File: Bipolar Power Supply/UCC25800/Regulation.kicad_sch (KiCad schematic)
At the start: 36 parts, among them U2 LT8330_S6, U4 LT8330_S6, U5 LM317EMPX/NOPB, U6 LM337IMPX/NOPB

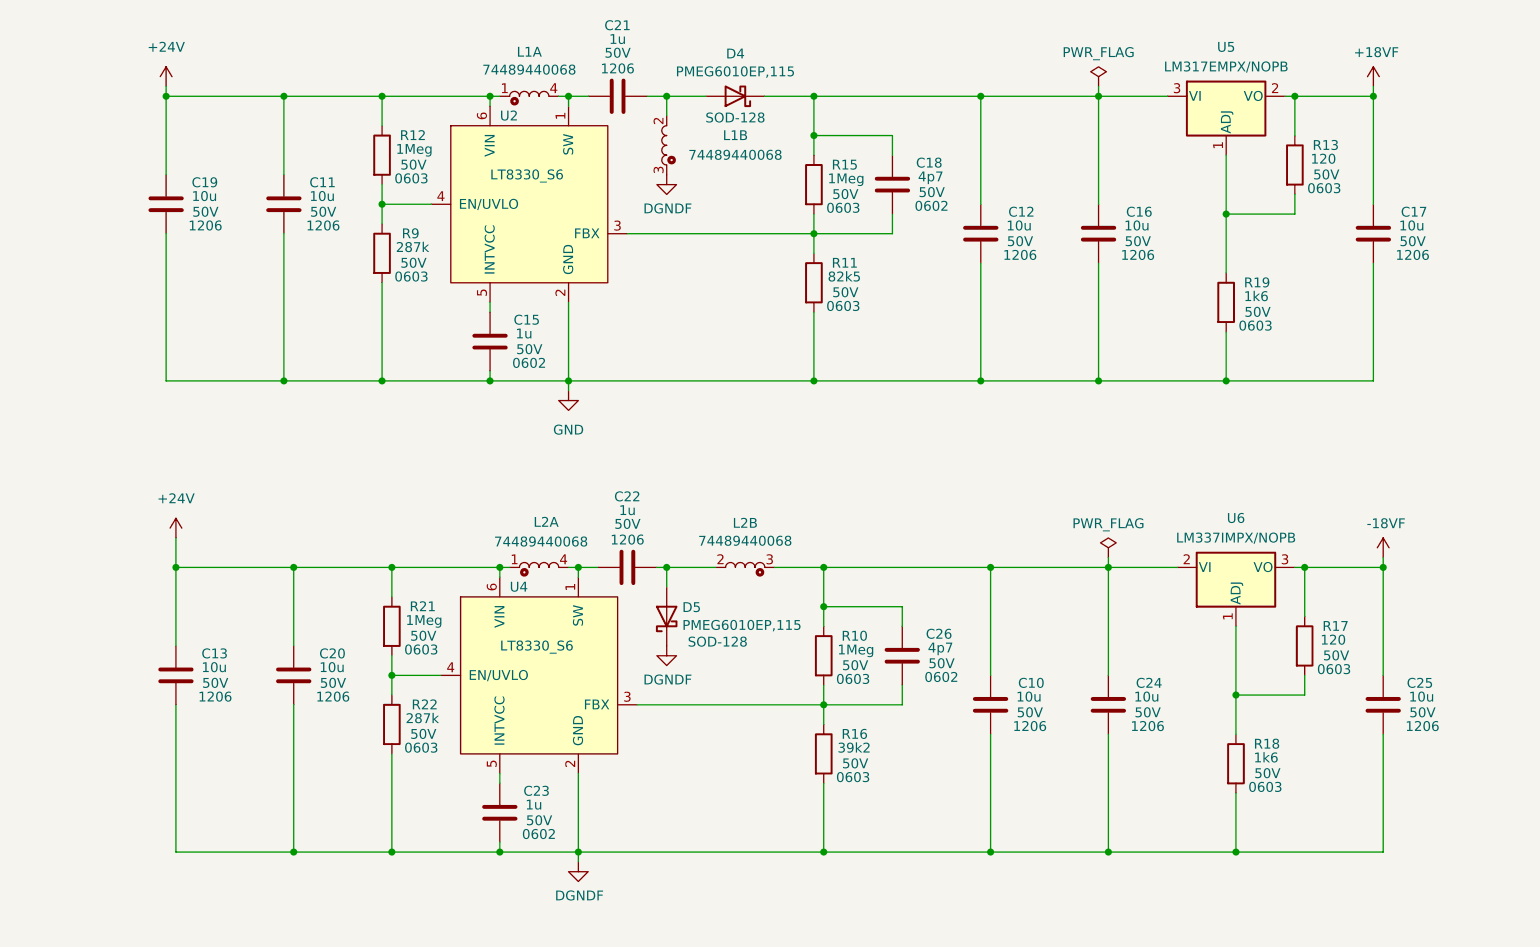
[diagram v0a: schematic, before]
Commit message: UCC25800 : Changes in sch and assignment of footprints.
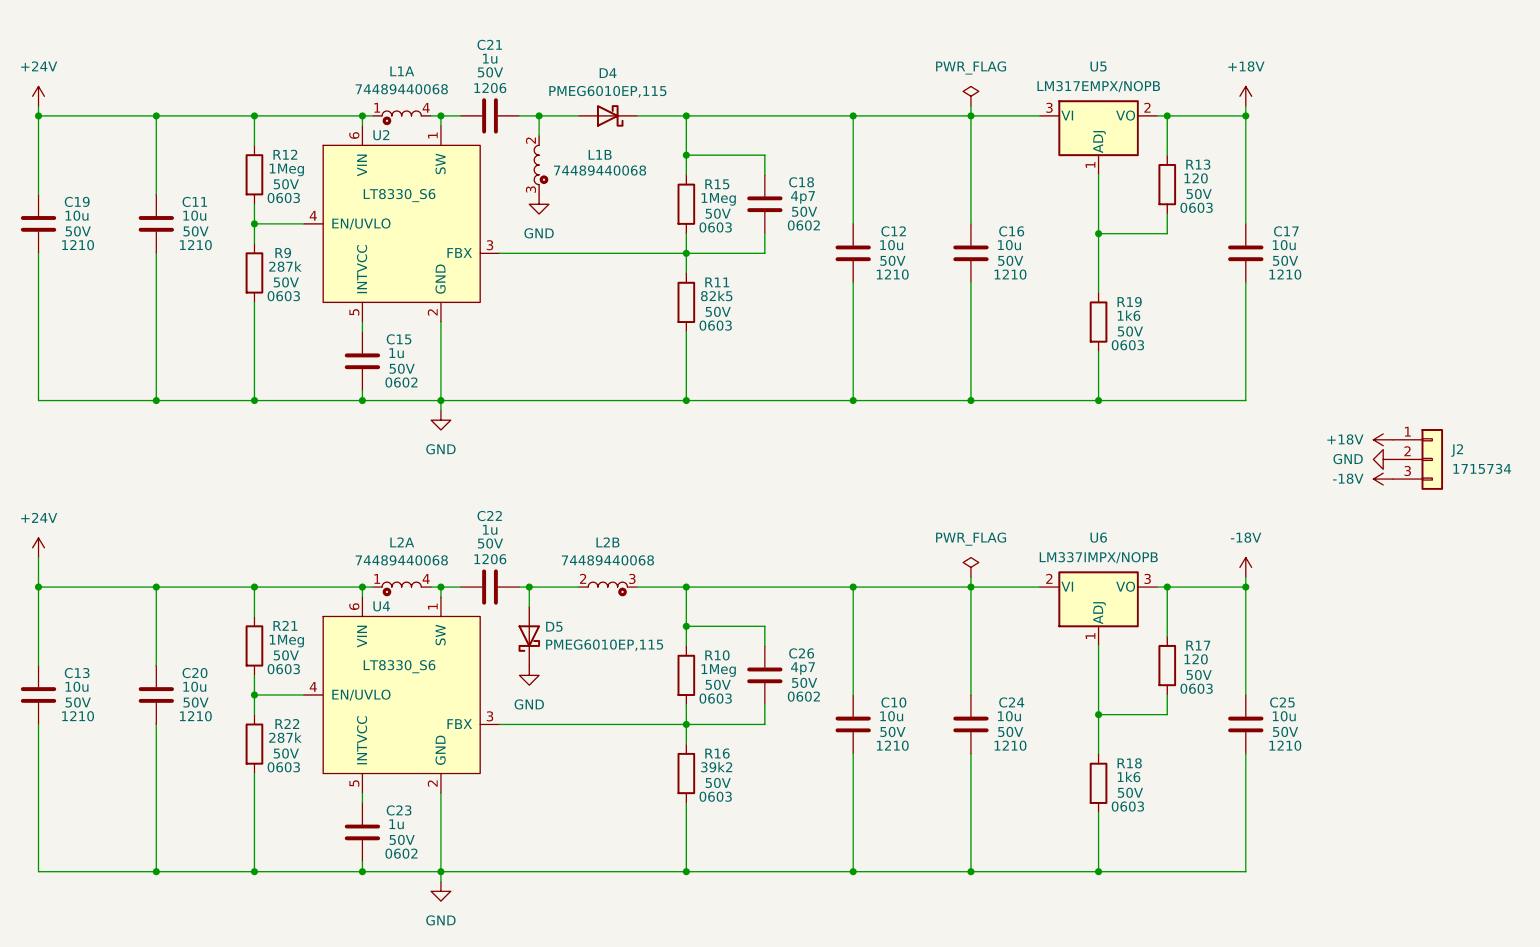
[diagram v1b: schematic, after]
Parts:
- added J2: 1715734, TerminalBlock_Phoenix:TerminalBlock_Phoenix_MKDS-1,5-3-5.08_1x03_P5.08mm_Horizontal, symbol Connector_Generic:Conn_01x03
- C10, C11, C12, C13, C16, C17, C19, C20, C24, C25: footprint (none) -> Capacitor_SMD:C_1210_3225Metric_Pad1.33x2.70mm_HandSolder; Package 1206 -> 1210
- C15, C18, C23, C26: footprint (none) -> Capacitor_SMD:C_0603_1608Metric_Pad1.08x0.95mm_HandSolder
- C21, C22: footprint (none) -> Capacitor_SMD:C_1206_3216Metric_Pad1.33x1.80mm_HandSolder
- D4, D5: Package SOD-128 -> (none)
- L1, L2: footprint (none) -> UCC25800:74489440068; symbol ADC_TEST:74489440068 -> UCC25800:74489440068
- R10, R11, R12, R13, R15, R16, R17, R18, R19, R21, R22, R9: footprint (none) -> Resistor_SMD:R_0603_1608Metric_Pad0.98x0.95mm_HandSolder
- U2, U4: symbol ADC_TEST:LT8330_S6 -> UCC25800:LT8330_S6
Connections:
- net DGNDF is gone; now on net GND: C10.2, C13.2, C20.2, C23.2, C24.2, C25.2, D5.1 (K), L1.3, R16.2, R18.2, R22.2, U4.2 (GND)
- net GND: now also J2.2 (Pin_2)
- net +18VF renamed +18V
- net +18V: now also J2.1 (Pin_1)
- net -18VF renamed -18V
- net -18V: now also J2.3 (Pin_3)
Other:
- moved on the sheet: C10, C11, C12, C13, C15, C16, C17, C18, C19, C20, C21, C22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
